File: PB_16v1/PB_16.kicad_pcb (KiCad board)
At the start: 2 copper layers, 148.1 x 102.6 mm, 85 parts, among them J1 String1, J10 String10, J11 String11, J12 String12, J13 String13, J14 String14, J15 String15, J16 String16, J17 Power In Left, J18 Power In Right, J19 USB, J2 String2, J20 DMX1 RJ45, J21 DMX2 RJ45, J22 DMX2, J23 VIN Voltage, J24 Expansion Header, J25 RTC Conn, J26 OLED Select, J27 GPIO Header, J28 Aux Pwr, J29 VIN Select, J3 String3, J4 String4, J5 String5, J6 String6, J7 String7, J8 String8, J9 String9, SW1 DMX_Renard_Select, SW2 OLED Select, SW3 DMX_LOR_Select, SW4 Enter BTN, SW5 Down BTN, U1 POCKETBEAGLE-SC-569, U2 Universe5V, U3 SN74HCT245N, U4 SN74HCT245N, U5 UA9638CP, U6 24L256

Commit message: switch footprint
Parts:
- SW1, SW2, SW3: footprint Button_Switch_THT:SW_CuK_JS202011CQN_DPDT_Straight -> Scotts:SW_CuK_JS202011CQN_DPDT_Straight
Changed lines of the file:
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@@
     )
   )
-  (footprint "Button_Switch_THT:SW_CuK_JS202011CQN_DPDT_Straight" (layer "F.Cu")
+  (footprint "Scotts:SW_CuK_JS202011CQN_DPDT_Straight" (layer "F.Cu")
     (at 115.6438 81.2766 -90)
     (descr "CuK sub miniature slide switch, JS series, DPDT, right angle, http://www.ckswitches.com/media/1422/js.pdf")
@@
     )
   )
-  (footprint "Button_Switch_THT:SW_CuK_JS202011CQN_DPDT_Straight" (layer "F.Cu")
+  (footprint "Scotts:SW_CuK_JS202011CQN_DPDT_Straight" (layer "F.Cu")
     (at 163.4962 56.3846 180)
     (descr "CuK sub miniature slide switch, JS series, DPDT, right angle, http://www.ckswitches.com/media/1422/js.pdf")
@@
     )
   )
-  (footprint "Button_Switch_THT:SW_CuK_JS202011CQN_DPDT_Straight" (layer "F.Cu")
+  (footprint "Scotts:SW_CuK_JS202011CQN_DPDT_Straight" (layer "F.Cu")
     (at 92.851 68.1678 180)
     (descr "CuK sub miniature slide switch, JS series, DPDT, right angle, http://www.ckswitches.com/media/1422/js.pdf")

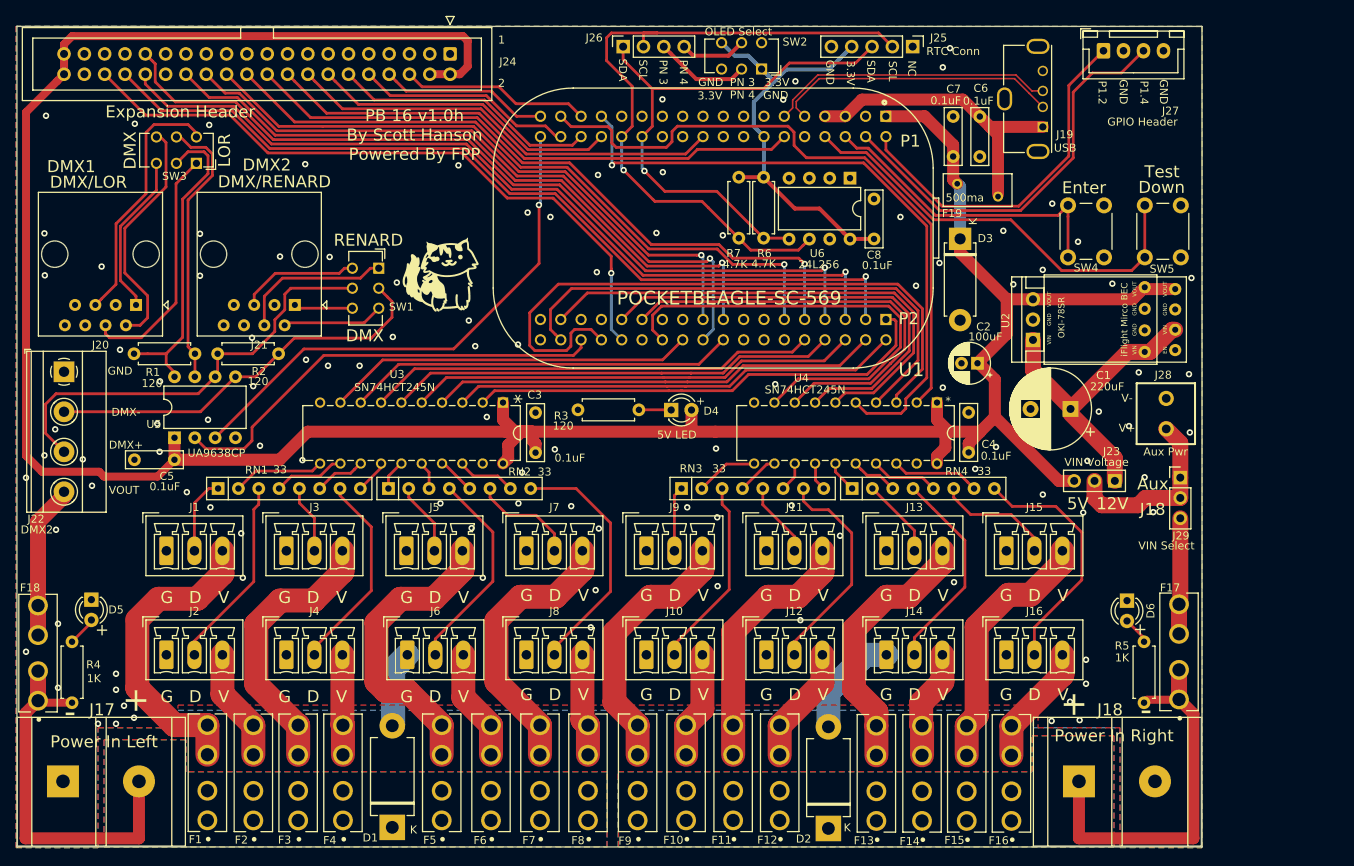
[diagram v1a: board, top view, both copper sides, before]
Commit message: update to kicad9
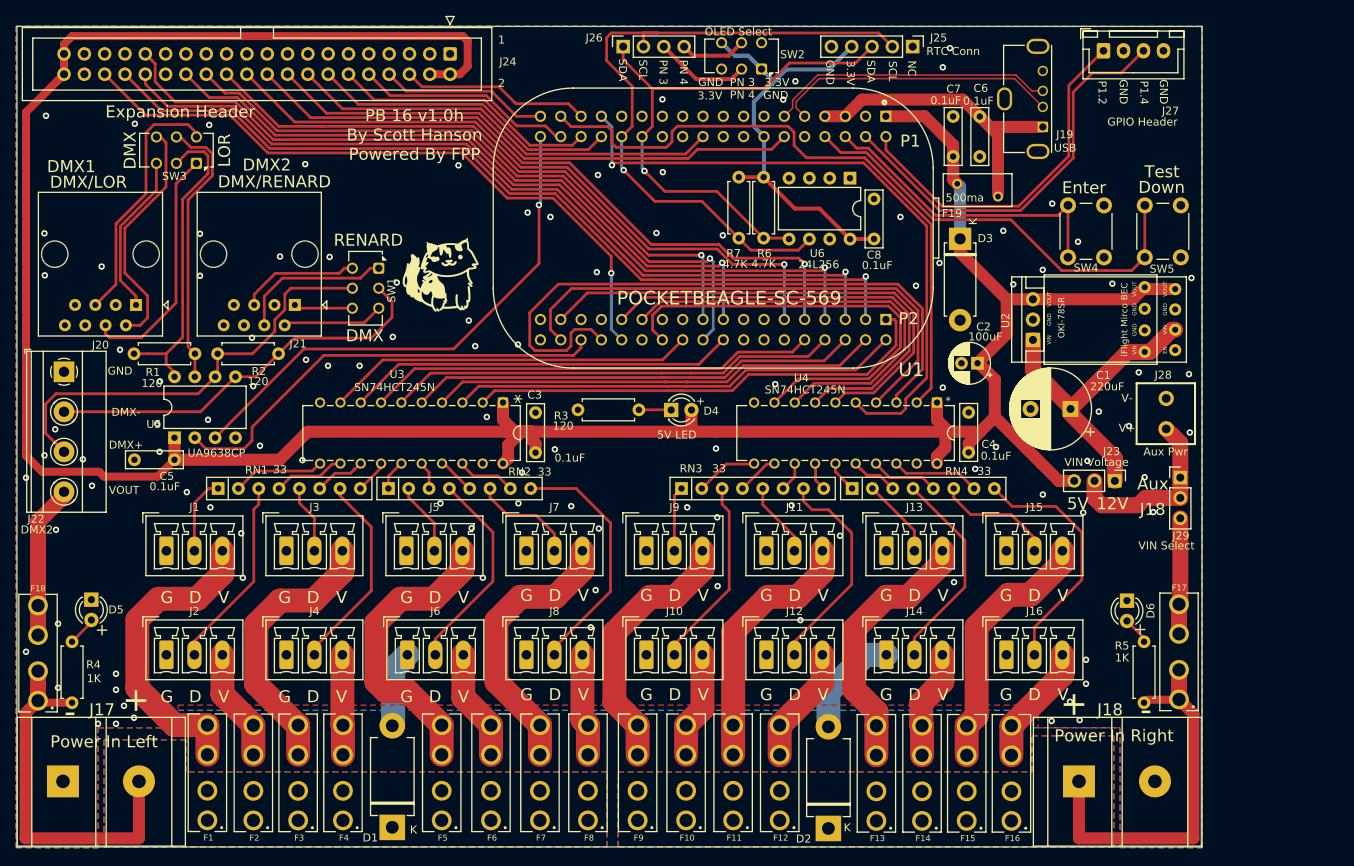
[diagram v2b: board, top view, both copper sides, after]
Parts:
- F1, F10, F11, F12, F13, F14, F15, F16, F17, F18, F2, F3, F4, F5, F6, F7, F8, F9: footprint Keystone_Fuse:FUSE_3544-2 -> Scotts:FUSE_3544-2
- SW1: footprint Scotts:SW_CuK_JS202011CQN_DPDT_Straight -> Button_Switch_THT:SW_CK_JS202011CQN_DPDT_Straight
- SW2, SW3: footprint Scotts:SW_CuK_JS202011CQN_DPDT_Straight -> Scotts:SW_CK_JS202011CQN_DPDT_Straight
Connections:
- J20 pad 2: Net-(SW3B-C) -> Net-(SW3B-A)
- J20 pad 5: Net-(SW3B-A) -> Net-(SW3B-C)
- J21 pad 1: Net-(SW1B-C) -> Net-(SW1B-A)
- J21 pad 5: Net-(SW1B-A) -> Net-(SW1B-C)
- SW2 pad 4: GND -> +3V3
- SW2 pad 6: +3V3 -> GND
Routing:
- net Net-(SW1B-C): track 7.34 -> 14.9 mm
- net Net-(SW1B-A): track 14.9 -> 7.34 mm
- net Net-(SW3B-C): track 29.3 -> 32.0 mm
- net Net-(SW3B-A): track 32.0 -> 29.3 mm

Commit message: add more
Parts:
- removed SW2: OLED Select, Scotts:SW_CK_JS202011CQN_DPDT_Straight
- added H1: MountingHole, Scotts:MountingHole_3.7mm, F.Cu at (233.7, 81.7)
- added H2: MountingHole, Scotts:MountingHole_3.7mm, F.Cu at (233.7, 90.6)
- added H3: MountingHole, Scotts:MountingHole_3.7mm, F.Cu at (233.7, 99.6)
- added H4: MountingHole, Scotts:MountingHole_3.7mm, F.Cu at (233.7, 108.5)
- added JP1: PIN_3_JMP, Scotts:SolderJumper-3_P1mm_Bridged12, F.Cu at (160.8, 56.3)
- added JP2: PIN_4_JMP, Scotts:SolderJumper-3_P1mm_Bridged23, F.Cu at (160.8, 54.1)
- J24: footprint Connector_IDC:IDC-Header_2x20_P2.54mm_Vertical -> Connector_IDC:IDC-Header_2x12_P2.54mm_Vertical
- SW3: footprint Scotts:SW_CK_JS202011CQN_DPDT_Straight -> Button_Switch_THT:SW_CK_JS202011CQN_DPDT_Straight
- moved J24 8.04 mm to (116.5, 54.5)
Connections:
- J24 pad 1: unconnected-(J24-Pin_1-Pad1) -> GND
- J24 pad 10: OUT19 -> OUT22
- J24 pad 11: GND -> OUT23
- J24 pad 12: OUT20 -> OUT24
- J24 pad 13: GND -> OUT25
- J24 pad 14: OUT21 -> OUT26
- J24 pad 15: GND -> OUT27
- J24 pad 16: OUT22 -> OUT28
- J24 pad 17: GND -> OUT29
- J24 pad 18: OUT23 -> OUT30
- J24 pad 19: GND -> OUT31
- J24 pad 2: +5V -> GND
- J24 pad 20: OUT24 -> OUT32
- J24 pad 21: GND -> unconnected-(J24-Pin_21-Pad21)
- J24 pad 22: OUT25 -> GND
- J24 pad 23: GND -> unconnected-(J24-Pin_23-Pad23)
- J24 pad 24: OUT26 -> unconnected-(J24-Pin_24-Pad24)
- J24 pad 3: GND -> +5V
- J24 pad 5: GND -> OUT17
- J24 pad 6: OUT17 -> OUT18
- J24 pad 7: GND -> OUT19
- J24 pad 8: OUT18 -> OUT20
- J24 pad 9: GND -> OUT21
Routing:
- net +5V: track 358.1 -> 340.2 mm
- net OUT32: track 83.7 -> 71.9 mm
- net OUT17: track 23.6 -> 33.7 mm
- net OUT30: track 104.8 -> 94.8 mm
- net OUT29: track 104.2 -> 94.3 mm
- net OUT19: track 27.2 -> 34.8 mm
- net OUT31: track 108.8 -> 101.3 mm
- net OUT28: track 84.3 -> 77.5 mm
- net OUT18: track 21.1 -> 26.6 mm
- net GND: track 23.2 -> 28.5 mm, vias 108 -> 116
- net OUT21: track 38.7 -> 43.8 mm
- net OUT26: track 76.8 -> 72.7 mm
- net OUT20: track 33.2 -> 36.3 mm
- net OUT23: track 67.6 -> 70.2 mm
- net OUT27: track 83.7 -> 81.4 mm
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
